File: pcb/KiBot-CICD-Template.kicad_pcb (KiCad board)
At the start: 4 copper layers, 30.5 x 17.8 mm, 0 parts

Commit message: modified kicad data
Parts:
- added R1: R, Resistor_SMD:R_0603_1608Metric, F.Cu at (121.4, 98.6)
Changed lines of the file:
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@@
   )
   (net 0 "")
+  (net 1 "Net-(R1-Pad1)")
+  (footprint "Resistor_SMD:R_0603_1608Metric" (layer "F.Cu")
+    (at 121.412 98.552)
+    (descr "Resistor SMD 0603 (1608 Metric), square (rectangular) end terminal, IPC_7351 nominal, (Body size source: IPC-SM-782 page 72, https://www.pcb-3d.com/wordpress/wp-content/uploads/ipc-sm-782a_amendment_1_and_2.pdf), generated with kicad-footprint-generator")
+    (tags "resistor")
+    (property "Sheetfile" "KiBot-CICD-Template.kicad_sch")
+    (property "Sheetname" "")
+    (property "Variant" "DNP")
+    (attr smd)
+    (fp_text reference "R1" (at 0 -1.43) (layer "F.SilkS")
+      (effects (font (size 1 1) (thickness 0.15)))
+    )
+    (fp_text value "R" (at 0 1.43) (layer "F.Fab")
+      (effects (font (size 1 1) (thickness 0.15)))
+    )
+    (fp_text user "${REFERENCE}" (at 0 0) (layer "F.Fab")
+      (effects (font (size 0.4 0.4) (thickness 0.06)))
+    )
+    (fp_line (start -0.237258 0.5225) (end 0.237258 0.5225) (layer "F.SilkS") (width 0.12))
+    (fp_line (start -0.237258 -0.5225) (end 0.237258 -0.5225) (layer "F.SilkS") (width 0.12))
+    (fp_line (start 1.48 -0.73) (end 1.48 0.73) (layer "F.CrtYd") (width 0.05))
+    (fp_line (start -1.48 0.73) (end -1.48 -0.73) (layer "F.CrtYd") (width 0.05))
+    (fp_line (start -1.48 -0.73) (end 1.48 -0.73) (layer "F.CrtYd") (width 0.05))
+    (fp_line (start 1.48 0.73) (end -1.48 0.73) (layer "F.CrtYd") (width 0.05))
+    (fp_line (start -0.8 0.4125) (end -0.8 -0.4125) (layer "F.Fab") (width 0.1))
+    (fp_line (start -0.8 -0.4125) (end 0.8 -0.4125) (layer "F.Fab") (width 0.1))
+    (fp_line (start 0.8 0.4125) (end -0.8 0.4125) (layer "F.Fab") (width 0.1))
+    (fp_line (start 0.8 -0.4125) (end 0.8 0.4125) (layer "F.Fab") (width 0.1))
+    (pad "1" smd roundrect (at -0.825 0) (size 0.8 0.95) (layers "F.Cu" "F.Paste" "F.Mask") (roundrect_rratio 0.25)
+      (net 1 "Net-(R1-Pad1)") (pintype "passive"))
+    (pad "2" smd roundrect (at 0.825 0) (size 0.8 0.95) (layers "F.Cu" "F.Paste" "F.Mask") (roundrect_rratio 0.25)
+      (net 1 "Net-(R1-Pad1)") (pintype "passive"))
+    (model "${KICAD6_3DMODEL_DIR}/Resistor_SMD.3dshapes/R_0603_1608Metric.wrl"
+      (offset (xyz 0 0 0))
+      (scale (xyz 1 1 1))
+      (rotate (xyz 0 0 0))
+    )
+  )
   (gr_arc (start 137.794999 104.139999) (mid 137.609012 104.589012) (end 137.159999 104.774999) (layer "Edge.Cuts") (width 0.1))
   (gr_arc (start 137.159999 86.994999) (mid 137.609012 87.180986) (end 137.794999 87.629999) (layer "Edge.Cuts") (width 0.1))

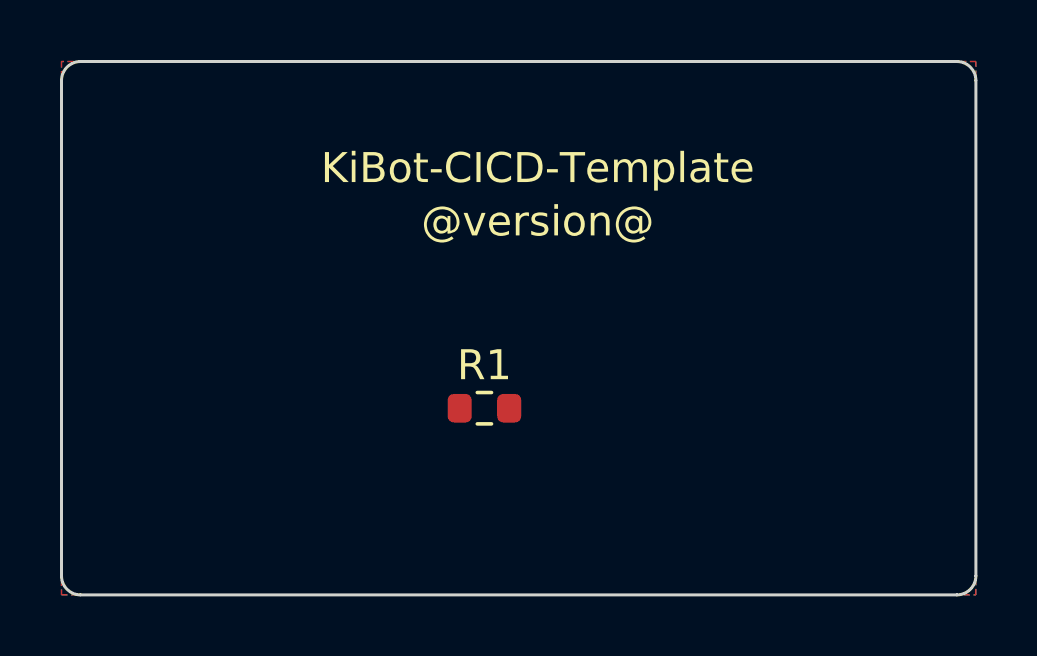
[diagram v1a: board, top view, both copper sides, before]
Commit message: route net
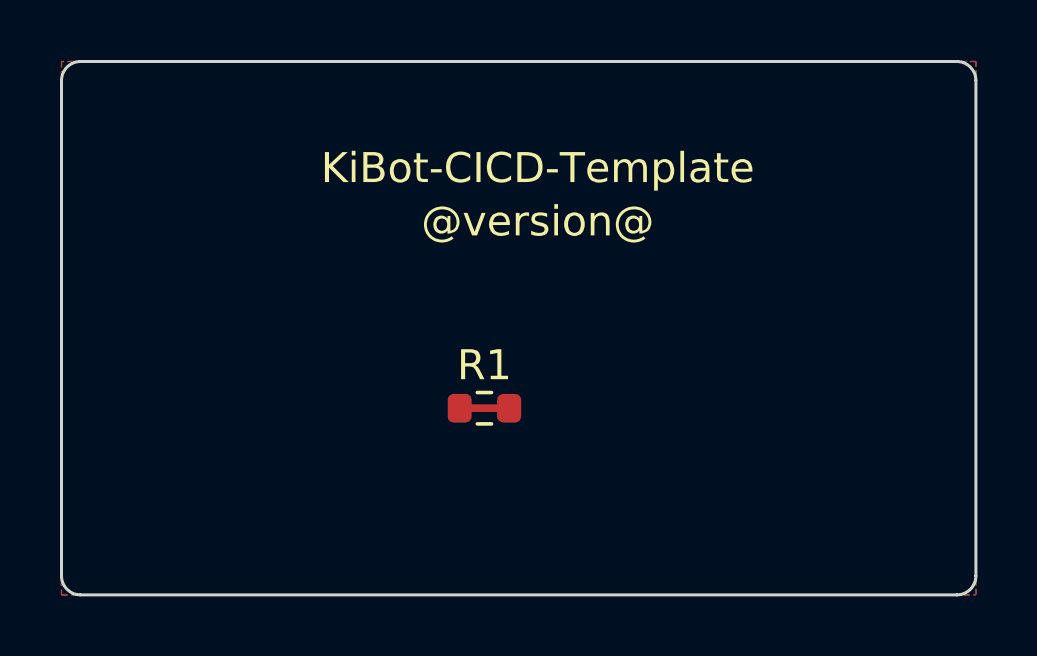
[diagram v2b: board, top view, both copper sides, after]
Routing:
- net Net-(R1-Pad1): track 0.00 -> 1.65 mm
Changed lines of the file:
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@@
     (style (thickness 0.15) (arrow_length 1.27) (text_position_mode 0) (extension_height 0.58642) (extension_offset 0) keep_text_aligned)
   )
+  (segment (start 120.587 98.552) (end 122.237 98.552) (width 0.25) (layer "F.Cu") (net 1))
   (zone (net 0) (net_name "") (layer "F.Cu") (hatch edge 0.508)
     (connect_pads (clearance 0.125))
